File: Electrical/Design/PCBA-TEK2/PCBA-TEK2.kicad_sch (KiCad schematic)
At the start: 0 parts

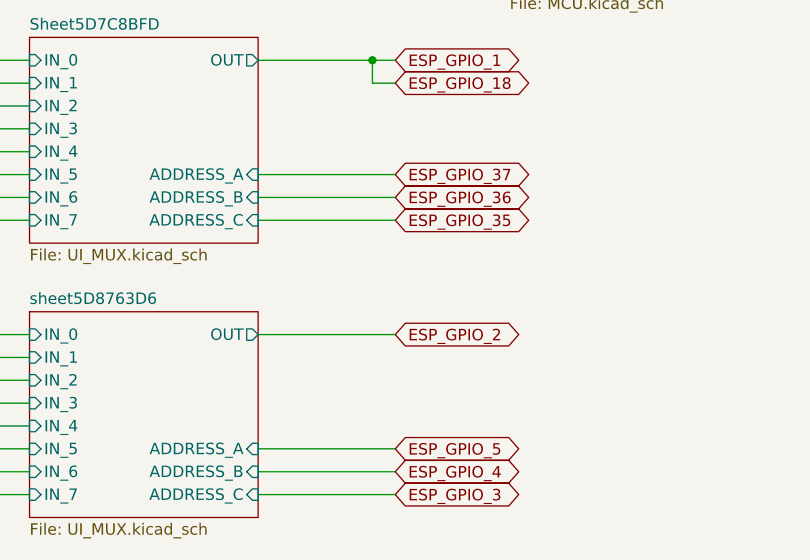
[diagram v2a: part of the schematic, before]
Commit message: SUKU debug adapter added to TEK2 classic
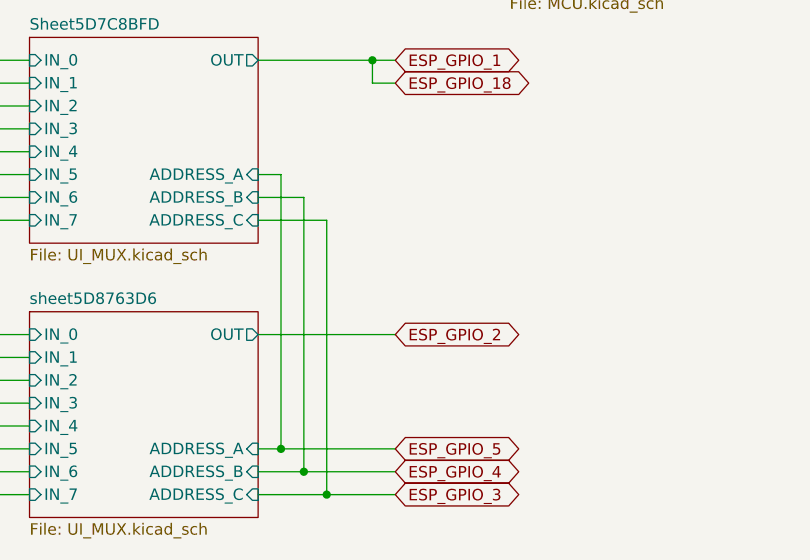
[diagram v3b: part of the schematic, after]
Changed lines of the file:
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@@
+		(color 0 0 0 0)
+	)
+	(junction
+		(at 203.2 228.6)
+		(diameter 0)
+		(color 0 0 0 0)
+	)
+	(junction
+		(at 205.74 231.14)
+		(diameter 0)
+		(color 0 0 0 0)
+	)
+	(junction
+		(at 208.28 233.68)
+		(diameter 0)
 		(color 0 0 0 0)
 	)
@@
 	(wire
 		(pts
+			(xy 205.74 231.14) (xy 215.9 231.14)
+		)
+		(stroke
+			(width 0)
+			(type default)
+		)
+	)
+	(wire
+		(pts
+			(xy 205.74 200.66) (xy 205.74 231.14)
+		)
+		(stroke
+			(width 0)
+			(type default)
+		)
+	)
+	(wire
+		(pts
 			(xy 127 101.6) (xy 132.08 101.6)
 		)
@@
 	(wire
 		(pts
+			(xy 203.2 228.6) (xy 215.9 228.6)
+		)
+		(stroke
+			(width 0)
+			(type default)
+		)
+	)
+	(wire
+		(pts
 			(xy 228.6 104.14) (xy 203.2 104.14)
 		)
@@
 	(wire
 		(pts
-			(xy 200.66 228.6) (xy 215.9 228.6)
+			(xy 200.66 228.6) (xy 203.2 228.6)
 		)
 		(stroke
@@
 	(wire
 		(pts
-			(xy 200.66 200.66) (xy 215.9 200.66)
+			(xy 203.2 198.12) (xy 203.2 228.6)
+		)
+		(stroke
+			(width 0)
+			(type default)
+		)
+	)
+	(wire
+		(pts
+			(xy 200.66 200.66) (xy 205.74 200.66)
 		)
 		(stroke
@@
 	(wire
 		(pts
-			(xy 200.66 233.68) (xy 215.9 233.68)
+			(xy 200.66 233.68) (xy 208.28 233.68)
 		)
 		(stroke
@@
 	(wire
 		(pts
-			(xy 200.66 231.14) (xy 215.9 231.14)
+			(xy 200.66 231.14) (xy 205.74 231.14)
 		)
 		(stroke
@@
 	(wire
 		(pts
+			(xy 208.28 233.68) (xy 215.9 233.68)
+		)
+		(stroke
+			(width 0)
+			(type default)
+		)
+	)
+	(wire
+		(pts
+			(xy 208.28 203.2) (xy 208.28 233.68)
+		)
+		(stroke
+			(width 0)
+			(type default)
+		)
+	)
+	(wire
+		(pts
 			(xy 127 104.14) (xy 132.08 104.14)
 		)
@@
 	(wire
 		(pts
-			(xy 200.66 198.12) (xy 215.9 198.12)
+			(xy 200.66 198.12) (xy 203.2 198.12)
 		)
 		(stroke
@@
 	(wire
 		(pts
-			(xy 200.66 203.2) (xy 215.9 203.2)
+			(xy 200.66 203.2) (xy 208.28 203.2)
 		)
 		(stroke
@@
 			)
 			(justify left bottom)
-		)
-	)
-	(global_label "ESP_GPIO_36"
-		(shape bidirectional)
-		(at 215.9 200.66 0)
-		(fields_autoplaced yes)
-		(effects
-			(font
-				(size 1.27 1.27)
-			)
-			(justify left)
-		)
-		(property "Intersheetrefs" "${INTERSHEET_REFS}"
-			(at 230.6823 200.5806 0)
-			(effects
-				(font
-					(size 1.27 1.27)
-				)
-				(justify left)
-				(hide yes)
-			)
-		)
-	)
-	(global_label "ESP_GPIO_37"
-		(shape bidirectional)
-		(at 215.9 198.12 0)
-		(fields_autoplaced yes)
-		(effects
-			(font
-				(size 1.27 1.27)
-			)
-			(justify left)
-		)
-		(property "Intersheetrefs" "${INTERSHEET_REFS}"
-			(at 230.6823 198.0406 0)
-			(effects
-				(font
-					(size 1.27 1.27)
-				)
-				(justify left)
-				(hide yes)
-			)
 		)
 	)
@@
 			(effects
 				(font
-					(size 1.27 1.27)
-				)
-				(justify left)
-				(hide yes)
-			)
-		)
-	)
-	(global_label "ESP_GPIO_35"
-		(shape bidirectional)
-		(at 215.9 203.2 0)
-		(fields_autoplaced yes)
-		(effects
-			(font
-				(size 1.27 1.27)
-			)
-			(justify left)
-		)
-		(property "Intersheetrefs" "${INTERSHEET_REFS}"
-			(at 230.6823 203.1206 0)
-			(effects
-				(font
